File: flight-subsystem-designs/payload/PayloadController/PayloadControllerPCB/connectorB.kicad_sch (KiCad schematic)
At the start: 2 parts, among them J2 FX10A-168P-SV71, J3 FX10A-168P-SV71

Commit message: Update plcl schematics
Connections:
- net GND: now reaches J3.1
- net GND: now also J3.11, J3.2
- no-connect marks 0 -> 6
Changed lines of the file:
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@@
 	(generator_version "9.0")
 	(paper "A4")
+	(junction
+		(at 44.45 45.72)
+		(diameter 0)
+		(color 0 0 0 0)
+	)
+	(no_connect
+		(at 46.99 63.5)
+	)
+	(no_connect
+		(at 46.99 53.34)
+	)
+	(no_connect
+		(at 46.99 60.96)
+	)
+	(no_connect
+		(at 46.99 55.88)
+	)
+	(no_connect
+		(at 46.99 50.8)
+	)
+	(no_connect
+		(at 46.99 66.04)
+	)
+	(wire
+		(pts
+			(xy 46.99 48.26) (xy 44.45 48.26)
+		)
+		(stroke
+			(width 0)
+			(type default)
+		)
+	)
+	(wire
+		(pts
+			(xy 43.18 71.12) (xy 46.99 71.12)
+		)
+		(stroke
+			(width 0)
+			(type default)
+		)
+	)
+	(wire
+		(pts
+			(xy 40.64 45.72) (xy 44.45 45.72)
+		)
+		(stroke
+			(width 0)
+			(type default)
+		)
+	)
+	(wire
+		(pts
+			(xy 44.45 48.26) (xy 44.45 45.72)
+		)
+		(stroke
+			(width 0)
+			(type default)
+		)
+	)
+	(wire
+		(pts
+			(xy 44.45 45.72) (xy 46.99 45.72)
+		)
+		(stroke
+			(width 0)
+			(type default)
+		)
+	)
 	(symbol
 		(lib_id "2025-10-26_15-21-50:FX10A-168P-SV71")
@@
 				)
 			)
+		)
+	)
+	(symbol
+		(lib_id "power:GND")
+		(at 40.64 45.72 0)
+		(unit 1)
+		(exclude_from_sim no)
+		(in_bom yes)
+		(on_board yes)
+		(dnp no)
+		(fields_autoplaced yes)
+		(property "Reference" "#PWR029"
+			(at 40.64 52.07 0)
+			(effects
+				(font
+					(size 1.27 1.27)
+				)
+				(hide yes)
+			)
+		)
+		(property "Value" "GND"
+			(at 40.64 50.8 0)
+			(effects
+				(font
+					(size 1.27 1.27)
+				)
+			)
+		)
+		(property "Footprint" ""
+			(at 40.64 45.72 0)
+			(effects
+				(font
+					(size 1.27 1.27)
+				)
+				(hide yes)
+			)
+		)
+		(property "Datasheet" ""
+			(at 40.64 45.72 0)
+			(effects
+				(font
+					(size 1.27 1.27)
+				)
+				(hide yes)
+			)
+		)
+		(property "Description" "Power symbol creates a global label with name \"GND\" , ground"
+			(at 40.64 45.72 0)
+			(effects
+				(font
+					(size 1.27 1.27)
+				)
+				(hide yes)
+			)
+		)
+		(pin "1"
+		)
+		(instances
+			(project ""
+				(path "/ab286999-0fbe-469b-b161-54b65f8cdf9b/989df9fc-9bfd-437a-be75-470077a57595"
+					(reference "#PWR029")
+					(unit 1)
+				)
+			)
+		)
+	)
+	(symbol
+		(lib_id "power:GND")
+		(at 43.18 71.12 0)
+		(unit 1)
+		(exclude_from_sim no)
+		(in_bom yes)
+		(on_board yes)
+		(dnp no)
+		(fields_autoplaced yes)
+		(property "Reference" "#PWR035"
+			(at 43.18 77.47 0)
+			(effects
+				(font
+					(size 1.27 1.27)
+				)
+				(hide yes)
+			)
+		)
+		(property "Value" "GND"
+			(at 43.18 76.2 0)
+			(effects
+				(font
+					(size 1.27 1.27)
+				)
+			)
+		)
+		(property "Footprint" ""
+			(at 43.18 71.12 0)
+			(effects
+				(font
+					(size 1.27 1.27)
+				)
+				(hide yes)
+			)
+		)
+		(property "Datasheet" ""
+			(at 43.18 71.12 0)
+			(effects
+				(font
+					(size 1.27 1.27)
+				)
+				(hide yes)
+			)
+		)
+		(property "Description" "Power symbol creates a global label with name \"GND\" , ground"
+			(at 43.18 71.12 0)
+			(effects
+				(font
+					(size 1.27 1.27)
+				)
+				(hide yes)
+			)
+		)
+		(pin "1"
+		)
+		(instances
+			(project "PayloadControllerPCB"
+				(path "/ab286999-0fbe-469b-b161-54b65f8cdf9b/989df9fc-9bfd-437a-be75-470077a57595"
+					(reference "#PWR035")
+					(unit 1)
+				)
+			)

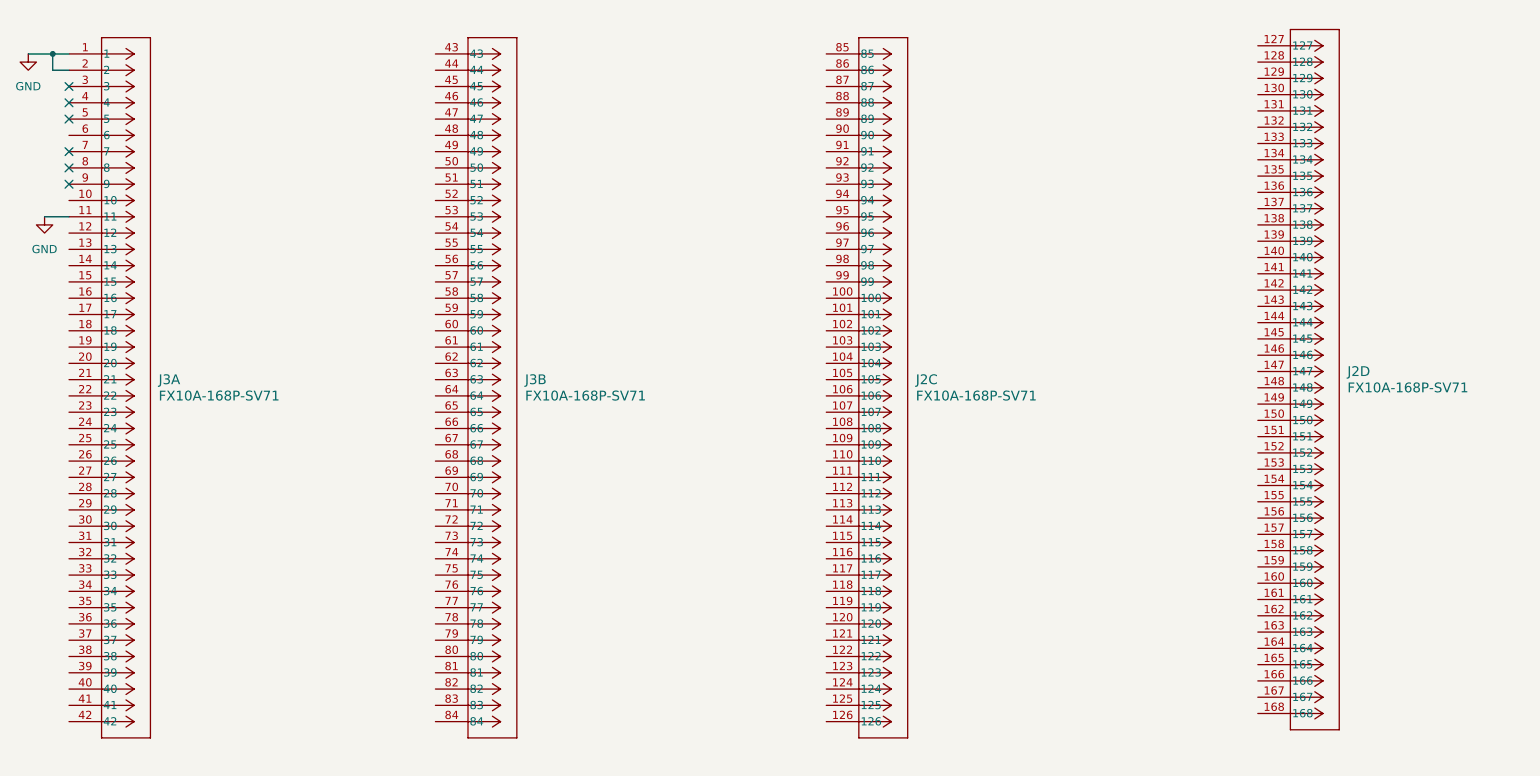
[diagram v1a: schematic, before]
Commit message: Update PC104 schematic
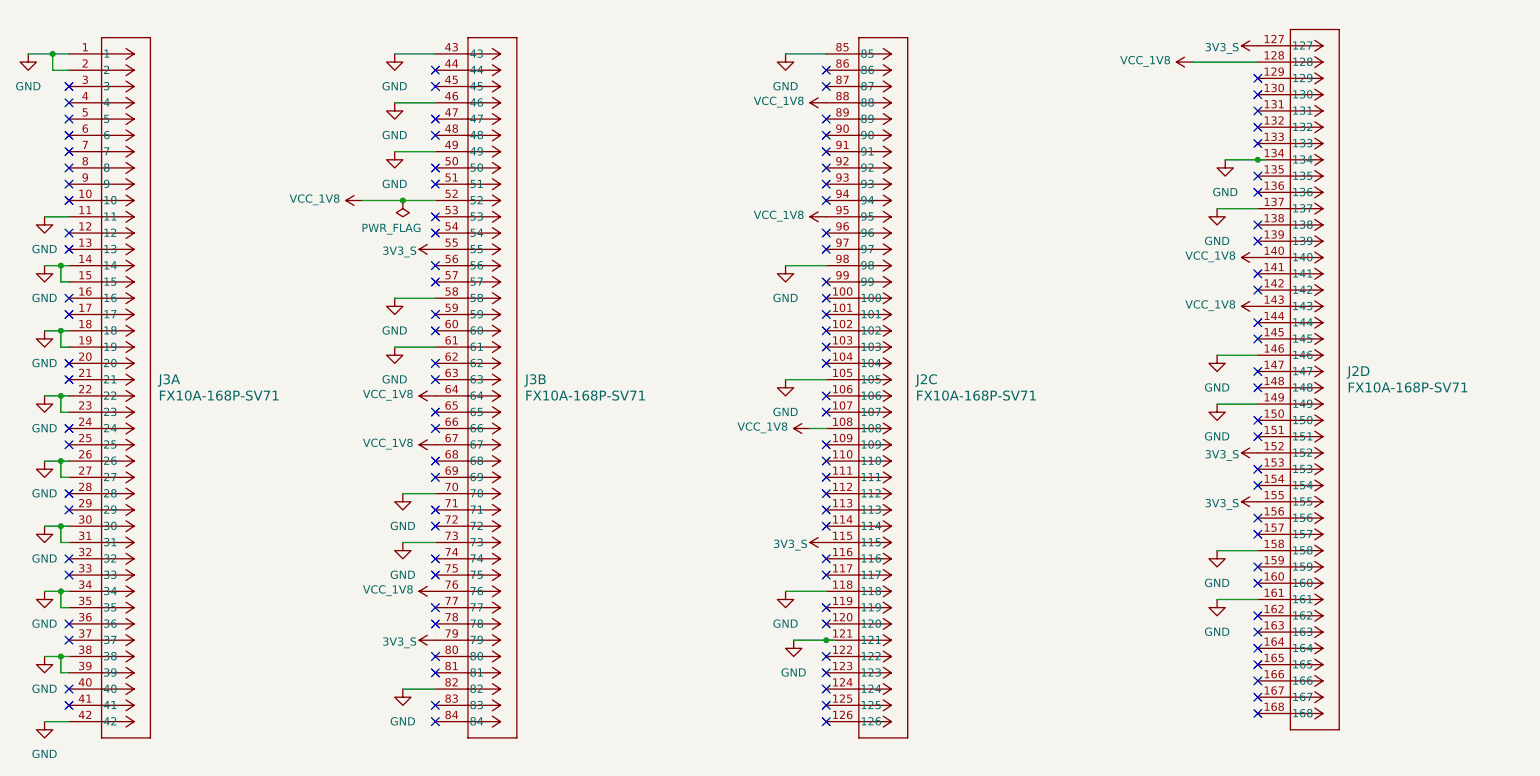
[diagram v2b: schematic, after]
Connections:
- net GND: now also J2.105, J2.118, J2.121, J2.134, J2.137, J2.146, J2.149, J2.158, J2.161, J2.85, J2.98, J3.14, J3.15, J3.18, J3.19, J3.22, J3.23, J3.26, J3.27, J3.30, J3.31, J3.34, J3.35, J3.38, J3.39, J3.42, J3.43, J3.46, J3.49, J3.58, J3.61, J3.70, J3.73, J3.82
- net 3V3_S: now reaches J2.127
- net 3V3_S: now also J2.115, J2.152, J2.155, J3.55, J3.79
- net VCC_1V8: now reaches J2.128
- net VCC_1V8: now also J2.108, J2.140, J2.143, J2.88, J2.95, J3.52, J3.64, J3.67, J3.76
- no-connect marks 6 -> 115

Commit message: Update PLCL Schematic
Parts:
- removed J3: FX10A-168P-SV71, CONN_FX10A-168P-SV71_HIR, symbol 2025-10-26_15-21-50:FX10A-168P-SV71
- added J1: FX10A-168P-SV71, CONN_FX10A-168P-SV71_HIR, symbol 2025-10-26_15-21-50:FX10A-168P-SV71
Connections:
- net 3V3_S: now also J1.55, J1.79
- net GND: now also J1.1, J1.11, J1.14, J1.15, J1.18, J1.19, J1.2, J1.22, J1.23, J1.26, J1.27, J1.30, J1.31, J1.34, J1.35, J1.38, J1.39, J1.42, J1.43, J1.46, J1.49, J1.58, J1.61, J1.70, J1.73, J1.82
- net VCC_1V8: now also J1.52, J1.64, J1.67, J1.76
- net BEACON_S+: now reaches J2.110
- net BEACON_S-: now reaches J2.112
- net MOSI: now reaches J2.90
- net MISO: now reaches J2.92
- net CS_N: now reaches J2.94
- new net DATA_LASERS_S+: J1.72
- new net DATA_LASERS_S-: J1.74
- new net FSM_EN: J1.81
- new net SCLK: J1.84
- no-connect marks 115 -> 107
